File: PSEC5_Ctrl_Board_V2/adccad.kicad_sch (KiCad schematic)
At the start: 16 parts, among them U2 LTC2600CGN_PBF, U4 LTC2600CGN_PBF, U7 MCP1501-25E/SN, U8 MCP1501-25E/SN

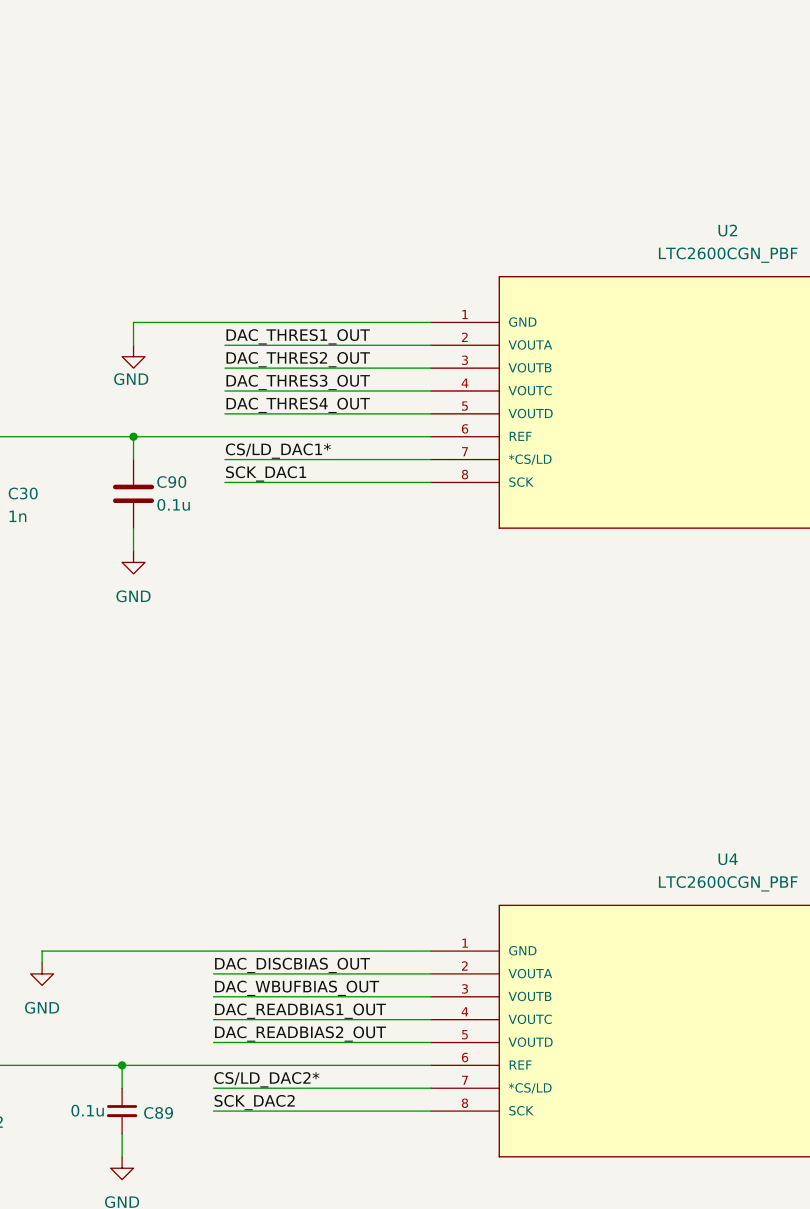
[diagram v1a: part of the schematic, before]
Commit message: silkscreen fixed, ready for check
V2 Board done, ready to order pre-check
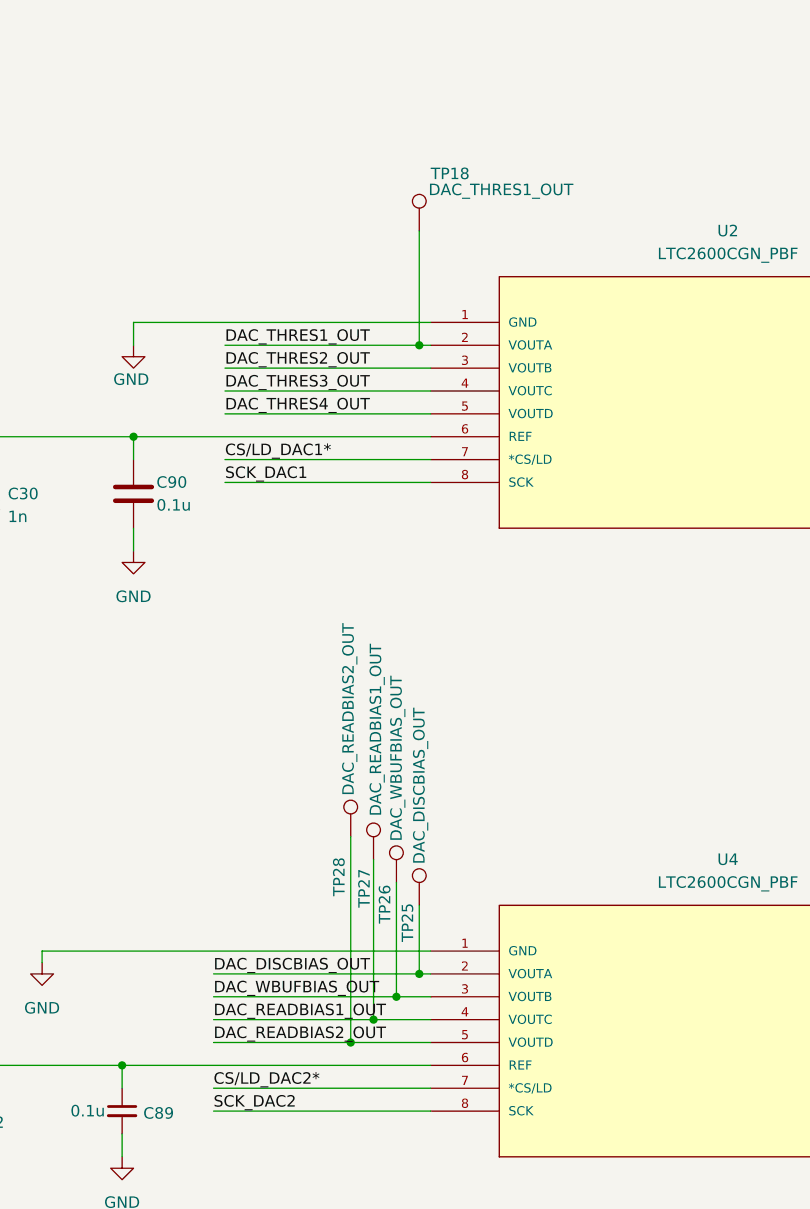
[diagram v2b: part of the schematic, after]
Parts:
- added TP18: DAC_THRES1_OUT, TestPoint:TestPoint_THTPad_1.5x1.5mm_Drill0.7mm, symbol Connector:TestPoint
- added TP25: DAC_DISCBIAS_OUT, TestPoint:TestPoint_THTPad_1.5x1.5mm_Drill0.7mm, symbol Connector:TestPoint
- added TP26: DAC_WBUFBIAS_OUT, TestPoint:TestPoint_THTPad_1.5x1.5mm_Drill0.7mm, symbol Connector:TestPoint
- added TP27: DAC_READBIAS1_OUT, TestPoint:TestPoint_THTPad_1.5x1.5mm_Drill0.7mm, symbol Connector:TestPoint
- added TP28: DAC_READBIAS2_OUT, TestPoint:TestPoint_THTPad_1.5x1.5mm_Drill0.7mm, symbol Connector:TestPoint
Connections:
- net DISCBIAS: now also TP25.1
- net Disc_Thresh1: now also TP18.1
- net READBIAS1: now also TP27.1
- net READBIAS2: now also TP28.1
- net WBUFBIAS: now also TP26.1

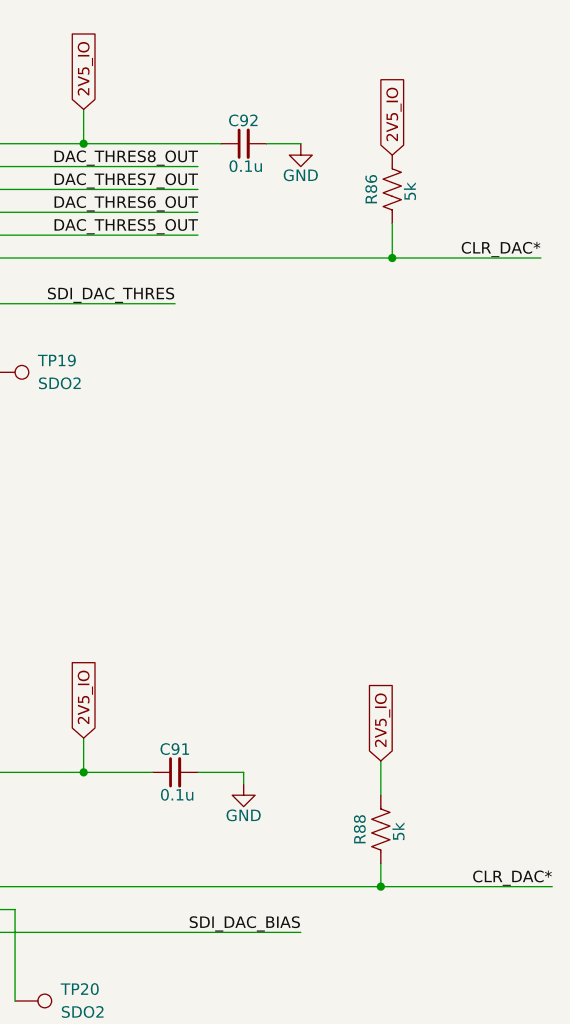
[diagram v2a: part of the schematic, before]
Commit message: Updated many values on schematic to match BOM
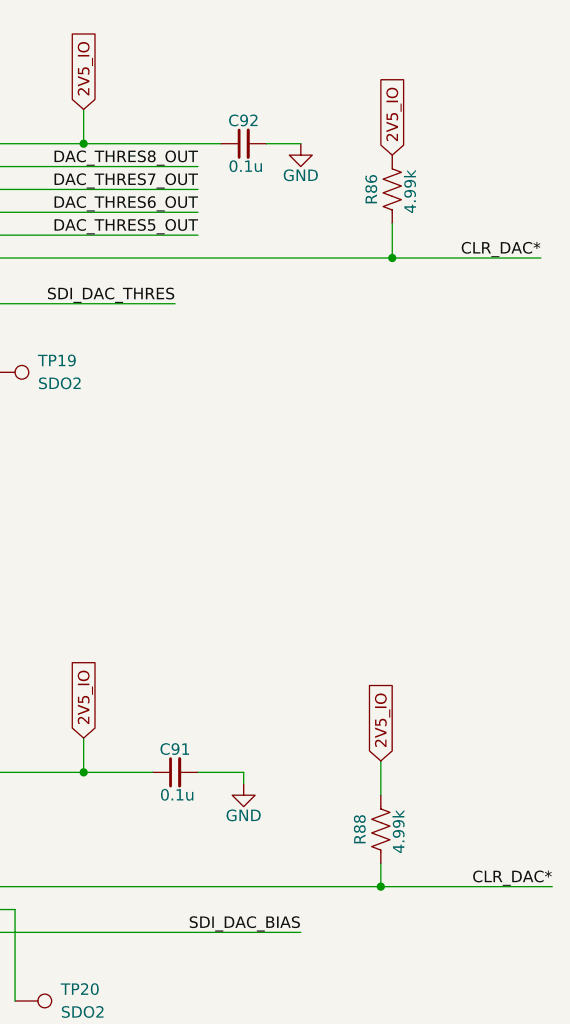
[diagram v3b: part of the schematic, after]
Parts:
- R86, R88: value 5k -> 4.99k
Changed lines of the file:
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@@
 			)
 		)
-		(property "Value" "5k"
+		(property "Value" "4.99k"
 			(at 388.112 68.834 90)
 			(effects
@@
 			)
 		)
-		(property "Value" "5k"
+		(property "Value" "4.99k"
 			(at 386.842 139.954 90)
 			(effects

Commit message: Updated kria
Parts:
- C89, C90: value 0.1u -> DNP
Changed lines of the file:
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@@
 			)
 		)
-		(property "Value" "0.1u"
+		(property "Value" "DNP"
 			(at 242.57 83.82 0)
 			(effects
@@
 			)
 		)
-		(property "Value" "0.1u"
+		(property "Value" "DNP"
 			(at 234.95 151.13 0)
 			(effects
